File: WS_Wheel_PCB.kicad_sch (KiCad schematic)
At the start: 6 parts, among them U1 Teensy4.1

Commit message: Making progress
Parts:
- added J1, J2, J3, J4: Conn_02x06_Counter_Clockwise, symbol Connector_Generic:Conn_02x06_Counter_Clockwise
- added MAX2, MAX3, MAX4: ~, Custom_Components:MAX3002, symbol custom_components:MAX3002
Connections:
- net at LS2.11 (Ay): now also LS3.3 (MISO), LS4.3 (MISO), J2.8 (Pin_8)
- net at LS2.12 (By): now also LS4.1 (SS/), MAX1.16 (Vcc4), J2.7 (Pin_7)
- net at LS2.16 (VDD): now also LS1.16 (VDD), LS3.16 (VDD), LS4.16 (VDD), MAX1.19 (Vcc), U1.48 (VIN), J1.1 (Pin_1), J2.1 (Pin_1), J3.1 (Pin_1), J4.1 (Pin_1)
- net at LS2.5 (Ax): now also J2.5 (Pin_5)
- net at LS2.6 (Bx): now also J2.6 (Pin_6)
- net at MAX1.12 (Vcc8): no longer U1.48 (VIN)
- net at LS1.11 (Ay): now also J3.8 (Pin_8)
- net at LS1.12 (By): now also J3.7 (Pin_7)
- net at LS1.5 (Ax): now also J3.5 (Pin_5)
- net at LS1.6 (Bx): now also J3.6 (Pin_6)
- net at LS3.11 (Ay): now also J1.8 (Pin_8)
- net at LS3.12 (By): now also J1.7 (Pin_7)
- net at LS3.5 (Ax): now also J1.5 (Pin_5)
- net at LS3.6 (Bx): now also J1.6 (Pin_6)
- net at U1.47 (GND): now also J1.12 (Pin_12), J2.12 (Pin_12), J3.12 (Pin_12), J4.12 (Pin_12)
- net at LS4.11 (Ay): now also J4.8 (Pin_8)
- net at LS4.12 (By): now also J4.7 (Pin_7)
- net at LS4.5 (Ax): now also J4.5 (Pin_5)
- net at LS4.6 (Bx): now also J4.6 (Pin_6)
- new net: J1.4 (Pin_4), MAX3.12 (Vcc8)
- new net: J1.3 (Pin_3), MAX3.13 (Vcc7)
- new net: J1.11 (Pin_11), MAX3.14 (Vcc6)
- new net: J1.2 (Pin_2), MAX3.15 (Vcc5)
- new net: J2.9 (Pin_9), MAX3.16 (Vcc4)
- new net: J2.4 (Pin_4), MAX3.17 (Vcc3)
- new net: J2.10 (Pin_10), MAX3.18 (Vcc2)
- new net: J2.3 (Pin_3), MAX3.20 (Vcc1)
- new net: J2.11 (Pin_11), MAX2.12 (Vcc8)
- new net: J2.2 (Pin_2), MAX2.13 (Vcc7)
- new net: J3.9 (Pin_9), MAX2.14 (Vcc6)
- new net: J3.4 (Pin_4), MAX2.15 (Vcc5)
- new net: J3.10 (Pin_10), MAX2.16 (Vcc4)
- new net: J3.3 (Pin_3), MAX2.17 (Vcc3)
- new net: J3.11 (Pin_11), MAX2.18 (Vcc2)
- new net: J3.2 (Pin_2), MAX2.20 (Vcc1)
- new net: J4.10 (Pin_10), MAX4.15 (Vcc5)
- new net: J4.11 (Pin_11), MAX4.16 (Vcc4)
- new net: J4.2 (Pin_2), MAX4.17 (Vcc3)
- new net: J4.3 (Pin_3), MAX4.13 (Vcc7)
- new net: J4.4 (Pin_4), MAX4.12 (Vcc8)
- new net: J4.9 (Pin_9), MAX4.14 (Vcc6)
- new net: J1.10 (Pin_10), MAX4.20 (Vcc1)
- new net: J1.9 (Pin_9), MAX4.18 (Vcc2)
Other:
- moved on the sheet: LS4, MAX1, U1

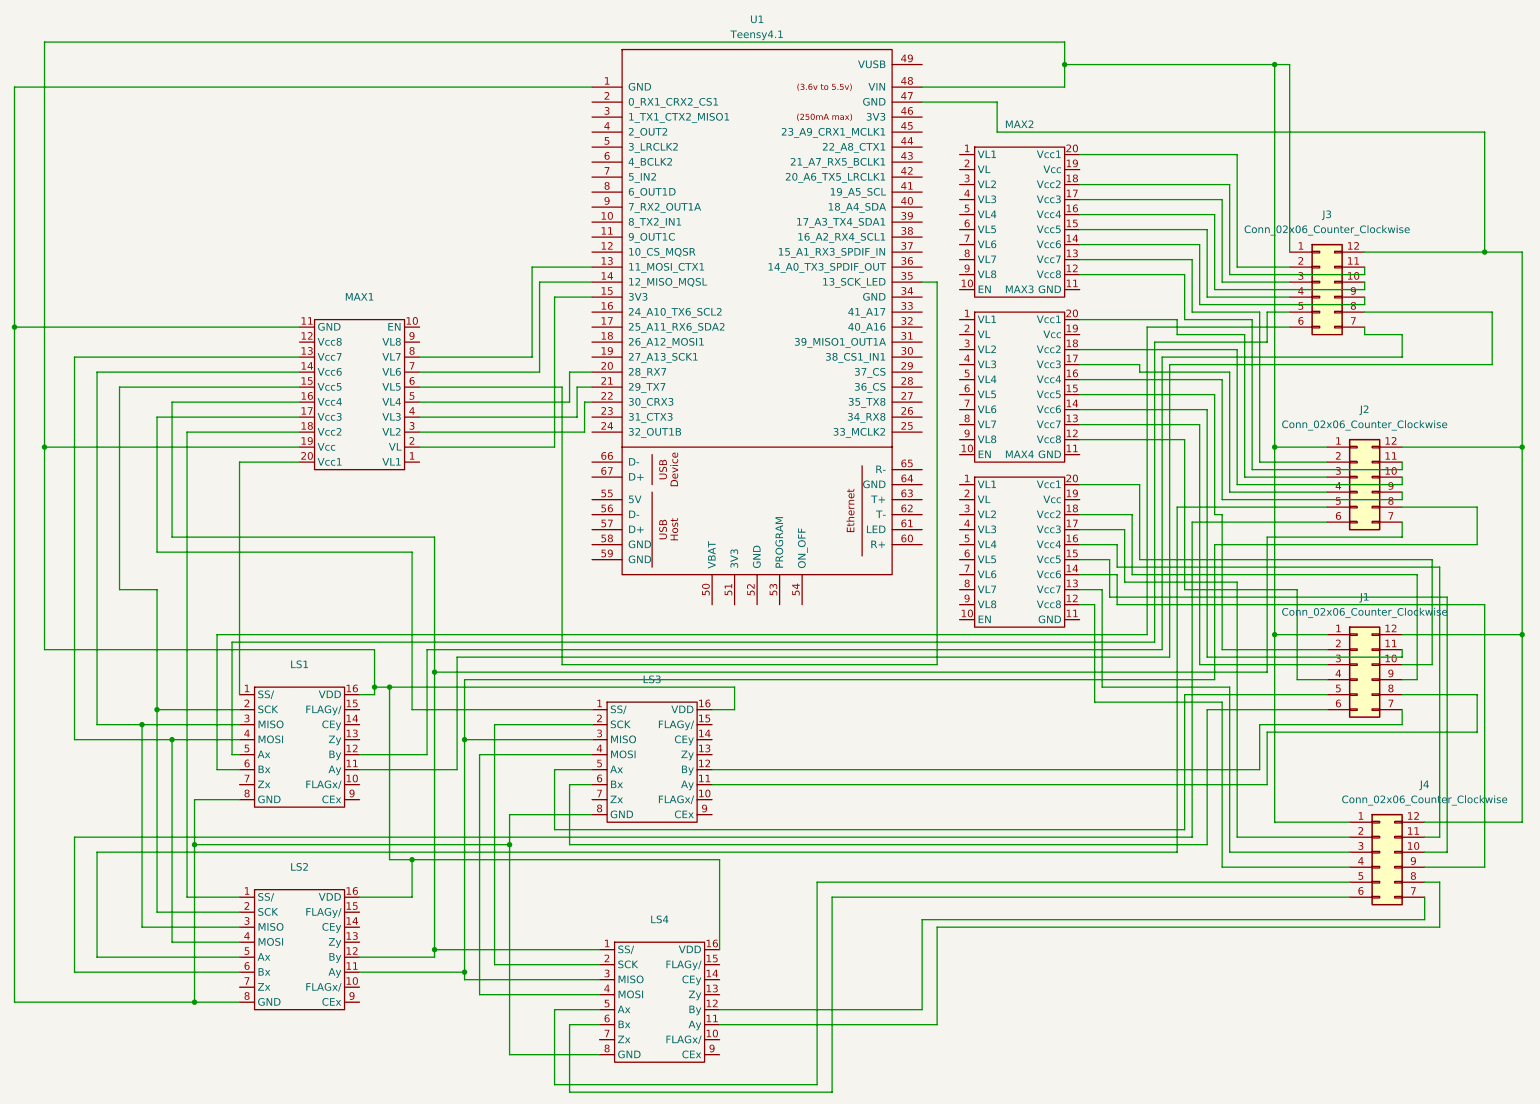
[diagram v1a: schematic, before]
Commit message: Starting over bc new voltage reqs
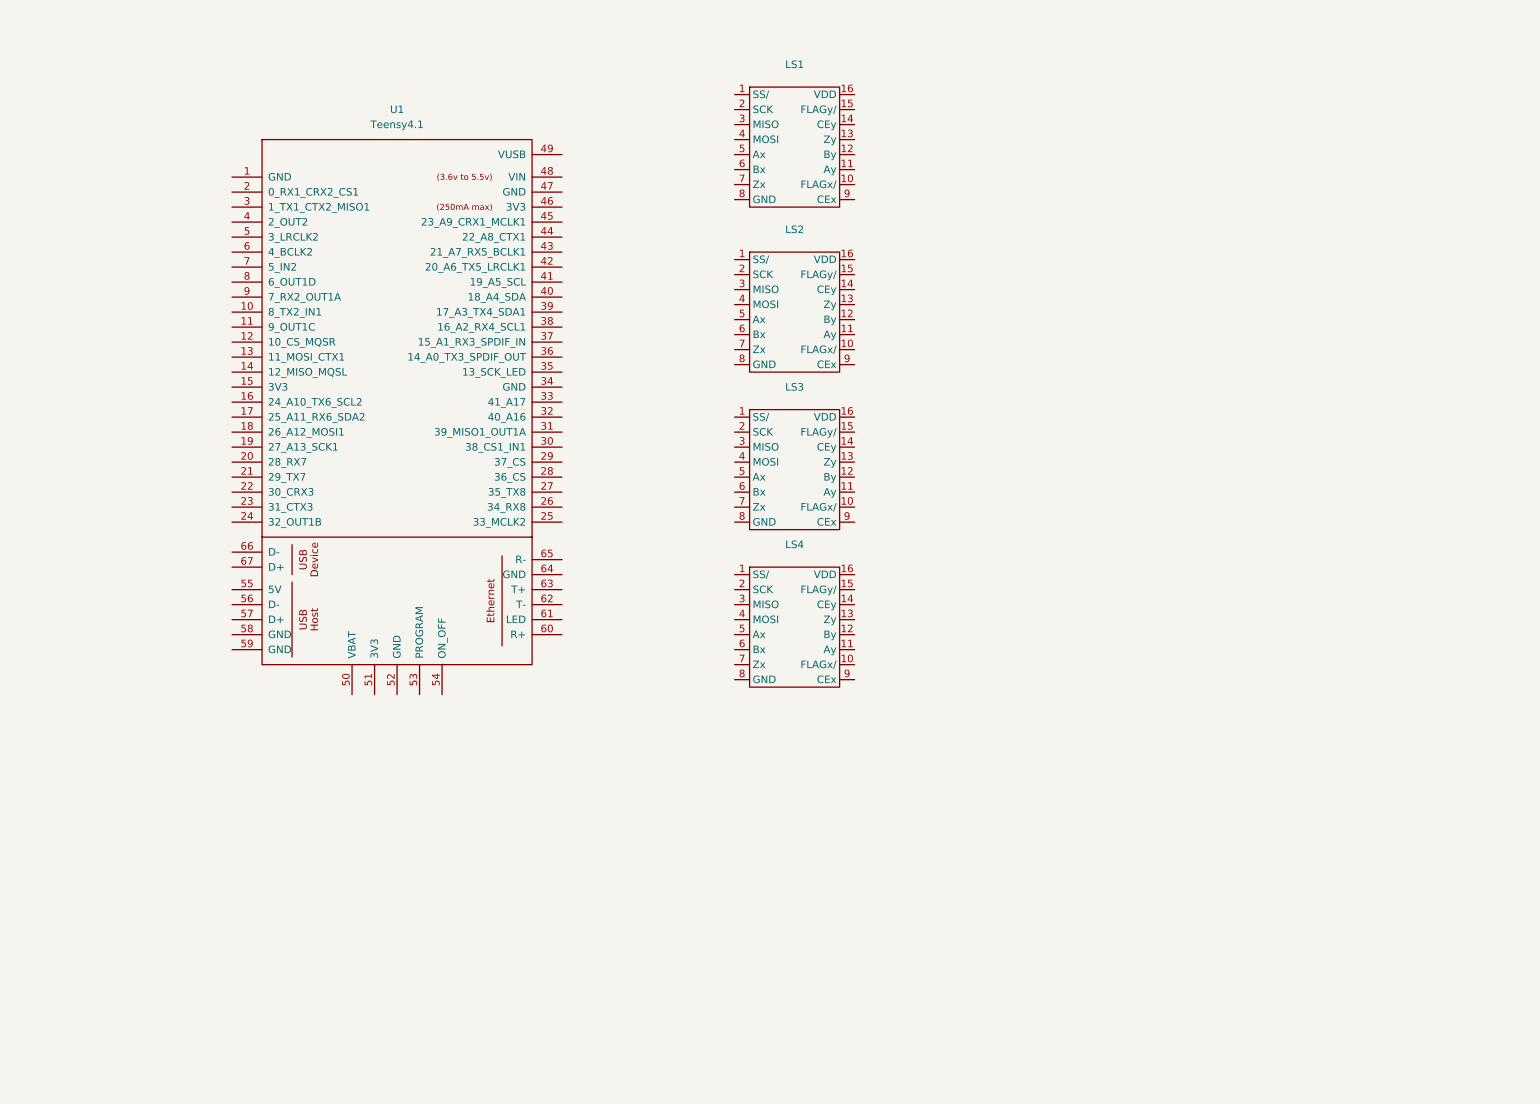
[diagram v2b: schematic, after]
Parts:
- removed J1, J2, J3, J4: Conn_02x06_Counter_Clockwise, symbol Connector_Generic:Conn_02x06_Counter_Clockwise
- removed MAX1, MAX2, MAX3, MAX4: ~, Custom_Components:MAX3002, symbol custom_components:MAX3002
- LS1, LS2, LS3, LS4: footprint Custom_Components:LS7466 -> (none)
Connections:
- net at LS4.1 (SS/): no longer LS2.12 (By)
- net at LS2.2 (SCK): no longer LS1.2 (SCK)
- net at LS2.3 (MISO): no longer LS1.3 (MISO)
- net at LS2.4 (MOSI): no longer LS1.4 (MOSI)
- net at LS3.2 (SCK): no longer LS4.2 (SCK)
- net at LS3.4 (MOSI): no longer LS4.4 (MOSI)
- now unconnected: LS1.16 (VDD), LS1.8 (GND), LS2.11 (Ay), LS2.16 (VDD), LS2.8 (GND), LS3.16 (VDD), LS3.3 (MISO), LS3.8 (GND), LS4.16 (VDD), LS4.3 (MISO), LS4.8 (GND), U1.1 (GND), U1.48 (VIN)
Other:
- moved on the sheet: U1

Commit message: Saving for the day
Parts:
- added C1, C2, C3, C4: ~, Connector_Molex:Molex_Nano-Fit_105310-xx12_2x06_P2.50mm_Vertical, symbol custom_components:Motor_Conn
- LS1, LS2, LS3, LS4: footprint (none) -> Custom_Components:LS7466
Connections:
- net at LS3.1 (SS/): now also U1.7 (5_IN2)
- net at LS3.11 (Ay): now also C3.11 (EncAy)
- net at LS3.12 (By): now also C3.12 (EncBy)
- net at LS3.16 (VDD): now also LS1.16 (VDD), LS2.16 (VDD), LS4.16 (VDD), U1.15 (3V3), C1.1 (3v3), C2.1 (3v3), C3.1 (3v3), C4.1 (3v3)
- net at LS3.2 (SCK): now also LS1.2 (SCK), LS2.2 (SCK), LS4.2 (SCK), U1.35 (13_SCK_LED)
- net at LS3.3 (MISO): now also LS1.3 (MISO), LS2.3 (MISO), LS4.3 (MISO), U1.14 (12_MISO_MQSL)
- net at LS3.4 (MOSI): now also LS1.4 (MOSI), LS2.4 (MOSI), LS4.4 (MOSI), U1.13 (11_MOSI_CTX1)
- net at LS3.5 (Ax): now also C3.5 (EncAx)
- net at LS3.6 (Bx): now also C3.6 (EncBx)
- net at LS3.8 (GND): now also LS1.8 (GND), LS2.8 (GND), LS4.8 (GND), U1.34 (GND), C1.7 (GND), C2.7 (GND), C3.7 (GND), C4.7 (GND)
- net at LS4.1 (SS/): now also U1.6 (4_BCLK2)
- net at LS4.11 (Ay): now also C4.11 (EncAy)
- net at LS4.12 (By): now also C4.12 (EncBy)
- net at LS4.5 (Ax): now also C4.5 (EncAx)
- net at LS4.6 (Bx): now also C4.6 (EncBx)
- net at LS2.1 (SS/): now also U1.5 (3_LRCLK2)
- net at LS2.11 (Ay): now also C2.11 (EncAy)
- net at LS2.12 (By): now also C2.12 (EncBy)
- net at LS2.5 (Ax): now also C2.5 (EncAx)
- net at LS2.6 (Bx): now also C2.4 (DirBx)
- net at U1.4 (2_OUT2): now also LS1.1 (SS/)
- net at LS1.11 (Ay): now also C1.11 (EncAy)
- net at LS1.12 (By): now also C1.12 (EncBy)
- net at LS1.5 (Ax): now also C1.5 (EncAx)
- net at LS1.6 (Bx): now also C1.6 (EncBx)
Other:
- moved on the sheet: LS1, LS2, LS3, LS4

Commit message: Final?
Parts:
- added Enc1, Enc2: ~, symbol custom_components:Quadrature_Encoder
- added J1: 5V in, Connector_Molex:Molex_Nano-Fit_105309-xx02_1x02_P2.50mm_Vertical, symbol Connector:Conn_01x02_Pin
- added M1, M2: Motor_DC, symbol Motor:Motor_DC
- added U2: ~, symbol custom_components:Motor_Conn
- added U3: ~, symbol custom_components:MotorDriver
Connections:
- net at C2.10 (DirBy): now also U1.18 (26_A12_MOSI1)
- net at C2.2 (ENx): now also U1.42 (20_A6_TX5_LRCLK1)
- net at C2.3 (DirAx): now also U1.41 (19_A5_SCL)
- net at C2.4 (DirBx): now also U1.40 (18_A4_SDA); no longer LS2.6 (Bx)
- net at C2.6 (EncBx): now also LS2.6 (Bx)
- net at C2.8 (ENy): now also U1.16 (24_A10_TX6_SCL2)
- net at C2.9 (DirAy): now also U1.17 (25_A11_RX6_SDA2)
- net at C3.10 (DirBy): now also U1.21 (29_TX7)
- net at C3.2 (ENx): now also U1.39 (17_A3_TX4_SDA1)
- net at C3.3 (DirAx): now also U1.38 (16_A2_RX4_SCL1)
- net at C3.4 (DirBx): now also U1.30 (38_CS1_IN1)
- net at C3.8 (ENy): now also U1.19 (27_A13_SCK1)
- net at C3.9 (DirAy): now also U1.20 (28_RX7)
- net at C1.10 (DirBy): now also U1.10 (8_TX2_IN1)
- net at C1.2 (ENx): now also U1.45 (23_A9_CRX1_MCLK1)
- net at C1.3 (DirAx): now also U1.44 (22_A8_CTX1)
- net at C1.4 (DirBx): now also U1.43 (21_A7_RX5_BCLK1)
- net at C1.8 (ENy): now also U1.8 (6_OUT1D)
- net at C1.9 (DirAy): now also U1.9 (7_RX2_OUT1A)
- net at U1.22 (30_CRX3): now also C4.8 (ENy)
- net at U1.23 (31_CTX3): now also C4.9 (DirAy)
- net at U1.24 (32_OUT1B): now also C4.10 (DirBy)
- net at U1.31 (39_MISO1_OUT1A): now also C4.4 (DirBx)
- net at U1.32 (40_A16): now also C4.3 (DirAx)
- net at U1.33 (41_A17): now also C4.2 (ENx)
- net at U1.47 (GND): now also J1.1 (Pin_1)
- net at U1.48 (VIN): now also J1.2 (Pin_2)
- new net: M2.1 (+), U3. (V_motor)
- new net: M2.2 (-), U3. (V_motor)
- new net: M1.1 (+), U3. (V_motor)
- new net: M1.2 (-), U3. (V_motor)
- new net: Enc1.1 (Vin), U2.1 (3v3), U3.1 (Vcc)
- new net: Enc2.4 (GND), U3.10 (GND)
- new net: U2.2 (ENx), U3.2 (P1)
- new net: U2.3 (DirAx), U3.3 (A1)
- new net: U2.4 (DirBx), U3.4 (B1)
- new net: Enc1.4 (GND), U2.7 (GND), U3.5 (GND)
- new net: Enc2.1 (Vin), U3.6 (Vcc)
- new net: U2.8 (ENy), U3.7 (P2)
- new net: U2.9 (DirAy), U3.8 (A2)
- new net: U2.10 (DirBy), U3.9 (B2)
- new net: Enc2.2 (A), U2.12 (EncBy)
- new net: Enc2.3 (B), U2.11 (EncAy)
- new net: Enc1.2 (A), U2.5 (EncAx)
- new net: Enc1.3 (B), U2.6 (EncBx)
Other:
- added sheet WiringHarness (harness.kicad_sch)
- note added: "Wheel PCB Connector Output"
- moved on the sheet: C1, C2, C3, C4, LS1, LS2, LS3, LS4, U1

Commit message: pushing
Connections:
- net at U3. (V_motor): now also M1.2 (-)
- net at U2.1 (3v3), U3.1 (Vcc): no longer Enc1.1 (Vin)
- net at Enc2.4 (GND), U3.10 (GND): now also Enc1.4 (GND)
- net at U2.7 (GND), U3.5 (GND): no longer Enc1.4 (GND)
- net at Enc2.1 (Vin), U3.6 (Vcc): now also Enc1.1 (Vin)
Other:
- note added: "(Dual) Wheel Motor Driver"
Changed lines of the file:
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@@
 	)
 	(junction
-		(at 148.59 278.13)
-		(diameter 0)
-		(color 0 0 0 0)
-	)
-	(junction
-		(at 140.97 267.97)
+		(at 187.96 278.13)
 		(diameter 0)
 		(color 0 0 0 0)
@@
 		(color 0 0 0 0)
 	)
+	(junction
+		(at 176.53 267.97)
+		(diameter 0)
+		(color 0 0 0 0)
+	)
 	(wire
 		(pts
@@
 	(wire
 		(pts
+			(xy 144.78 264.16) (xy 176.53 264.16)
+		)
+		(stroke
+			(width 0)
+			(type default)
+		)
+	)
+	(wire
+		(pts
 			(xy 193.04 68.58) (xy 251.46 68.58)
 		)
@@
 	(wire
 		(pts
+			(xy 176.53 267.97) (xy 172.72 267.97)
+		)
+		(stroke
+			(width 0)
+			(type default)
+		)
+	)
+	(wire
+		(pts
 			(xy 123.19 102.87) (xy 120.65 102.87)
 		)
@@
 	(wire
 		(pts
+			(xy 165.1 308.61) (xy 165.1 304.8)
+		)
+		(stroke
+			(width 0)
+			(type default)
+		)
+	)
+	(wire
+		(pts
 			(xy 57.15 67.31) (xy 57.15 45.72)
 		)
@@
 	(wire
 		(pts
-			(xy 151.13 306.07) (xy 151.13 299.72)
-		)
-		(stroke
-			(width 0)
-			(type default)
-		)
-	)
-	(wire
-		(pts
 			(xy 177.8 72.39) (xy 223.52 72.39)
 		)
@@
 	(wire
 		(pts
-			(xy 148.59 299.72) (xy 148.59 278.13)
-		)
-		(stroke
-			(width 0)
-			(type default)
-		)
-	)
-	(wire
-		(pts
 			(xy 157.48 327.66) (xy 140.97 327.66)
 		)
@@
 	(wire
 		(pts
-			(xy 241.3 123.19) (xy 260.35 123.19)
+			(xy 191.77 304.8) (xy 191.77 278.13)
 		)
 		(stroke
@@
 	(wire
 		(pts
-			(xy 119.38 260.35) (xy 185.42 260.35)
+			(xy 152.4 308.61) (xy 165.1 308.61)
 		)
 		(stroke
@@
 	(wire
 		(pts
-			(xy 148.59 278.13) (xy 157.48 278.13)
+			(xy 241.3 123.19) (xy 260.35 123.19)
+		)
+		(stroke
+			(width 0)
+			(type default)
+		)
+	)
+	(wire
+		(pts
+			(xy 119.38 260.35) (xy 185.42 260.35)
 		)
 		(stroke
@@
 	(wire
 		(pts
-			(xy 187.96 257.81) (xy 187.96 275.59)
+			(xy 176.53 264.16) (xy 176.53 267.97)
 		)
 		(stroke
@@
 	(wire
 		(pts
-			(xy 260.35 97.79) (xy 260.35 95.25)
+			(xy 187.96 257.81) (xy 187.96 275.59)
 		)
 		(stroke
@@
 	(wire
 		(pts
-			(xy 207.01 128.27) (xy 128.27 128.27)
+			(xy 260.35 97.79) (xy 260.35 95.25)
 		)
 		(stroke
@@
 	(wire
 		(pts
-			(xy 140.97 308.61) (xy 140.97 267.97)
+			(xy 207.01 128.27) (xy 128.27 128.27)
 		)
 		(stroke
@@
 	(wire
 		(pts
+			(xy 191.77 278.13) (xy 187.96 278.13)
+		)
+		(stroke
+			(width 0)
+			(type default)
+		)
+	)
+	(wire
+		(pts
 			(xy 177.8 36.83) (xy 177.8 41.91)
 		)
@@
 	(wire
 		(pts
-			(xy 54.61 267.97) (xy 140.97 267.97)
-		)
-		(stroke
-			(width 0)
-			(type default)
-		)
-	)
-	(wire
-		(pts
 			(xy 198.12 50.8) (xy 198.12 52.07)
 		)
@@
 	(wire
 		(pts
-			(xy 152.4 306.07) (xy 151.13 306.07)
-		)
-		(stroke
-			(width 0)
-			(type default)
-		)
-	)
-	(wire
-		(pts
 			(xy 100.33 287.02) (xy 78.74 287.02)
 		)
@@
 	(wire
 		(pts
-			(xy 133.35 278.13) (xy 148.59 278.13)
+			(xy 133.35 278.13) (xy 157.48 278.13)
 		)
 		(stroke
@@
 	(wire
 		(pts
-			(xy 152.4 308.61) (xy 152.4 306.07)
-		)
-		(stroke
-			(width 0)
-			(type default)
-		)
-	)
-	(wire
-		(pts
 			(xy 184.15 62.23) (xy 128.27 62.23)
 		)
@@
 	(wire
 		(pts
-			(xy 144.78 308.61) (xy 140.97 308.61)
-		)
-		(stroke
-			(width 0)
-			(type default)
-		)
-	)
-	(wire
-		(pts
 			(xy 248.92 82.55) (xy 241.3 82.55)
 		)
@@
 	(wire
 		(pts
-			(xy 151.13 299.72) (xy 148.59 299.72)
-		)
-		(stroke
-			(width 0)
-			(type default)
-		)
-	)
-	(wire
-		(pts
 			(xy 125.73 19.05) (xy 125.73 57.15)
 		)
@@
 	(wire
 		(pts
+			(xy 165.1 304.8) (xy 191.77 304.8)
+		)
+		(stroke
+			(width 0)
+			(type default)
+		)
+	)
+	(wire
+		(pts
 			(xy 153.67 41.91) (xy 54.61 41.91)
 		)
@@
 	(wire
 		(pts
-			(xy 140.97 267.97) (xy 157.48 267.97)
+			(xy 54.61 267.97) (xy 157.48 267.97)
 		)
 		(stroke
@@
 	(wire
 		(pts
-			(xy 180.34 267.97) (xy 172.72 267.97)
+			(xy 180.34 267.97) (xy 176.53 267.97)
 		)
 		(stroke
@@
 	(wire
 		(pts
+			(xy 144.78 308.61) (xy 144.78 264.16)
+		)
+		(stroke
+			(width 0)
+			(type default)
+		)
+	)
+	(wire
+		(pts
 			(xy 177.8 104.14) (xy 203.2 104.14)
 		)
@@
 		)
 	)
+	(text "(Dual) Wheel Motor Driver"
+		(exclude_from_sim no)
+		(at 165.608 283.718 0)
+		(effects
+			(font
+				(size 1.27 1.27)
+			)
+		)
+	)
